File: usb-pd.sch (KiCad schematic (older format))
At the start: 39 parts, among them J12 12401598E4_2A, Q7 SQS401EN-T1_BE3, U18 STUSB4500QTR

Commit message: Reorganize schematics, add descriptions in top left corner
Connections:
- wire segments 133 -> 131
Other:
- note added: "USB-C PD controller"
- note removed: "R G B\n50 30 30 [mA]\n2.1 2.9 2.9 [V]"
- moved on the sheet: C127, C128, C136, C137, C138, C139, D1, D23, D24, D27, D31, J12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

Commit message: Increase spacing between D27 and U18, reduce D27 brightness to ~20%
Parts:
- removed R131: R_100R_0402, sa800u-baseboard-hw-footprints:0402-res, symbol sa800u-baseboard-hw:R_100R_0402
- removed R132: R_150R_0402, sa800u-baseboard-hw-footprints:0402-res, symbol sa800u-baseboard-hw:R_150R_0402
- removed R133: R_590R_0402, sa800u-baseboard-hw-footprints:0402-res, symbol sa800u-baseboard-hw:R_590R_0402
- added R131: R_510R_0402, sa800u-baseboard-hw-footprints:0402-res, symbol sa800u-baseboard-hw:R_510R_0402
- added R132: R_750R_0402, sa800u-baseboard-hw-footprints:0402-res, symbol sa800u-baseboard-hw:R_750R_0402
- added R133: R_2k7_0402, sa800u-baseboard-hw-footprints:0402-res, symbol sa800u-baseboard-hw:R_2k7_0402
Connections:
- wire segments 131 -> 132
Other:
- moved on the sheet: D27
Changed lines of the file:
@@
 Wire Wire Line
 	10225 5525 10225 5900
-Wire Wire Line
-	10925 6825 10925 7050
-Wire Wire Line
-	10725 6825 10725 6950
 $Comp
 L sa800u-baseboard-hw:ASMB-TTF0-0A20B D27
 U 1 1 620BAED1
-P 10925 6175
-F 0 "D27" V 10872 6553 60  0000 L CNN
-F 1 "ASMB-TTF0-0A20B" V 10978 6553 60  0000 L CNN
-F 2 "sa800u-baseboard-hw-footprints:PLCC6_3.5x3.7mm" H 10525 5475 60  0001 L CNN
-F 3 "https://docs.broadcom.com/doc/ASMB-TTF0-0A20B-DS101" H 11125 6475 60  0001 L CNN
-F 4 "ASMB-TTF0-0A20B" H 10475 5575 60  0001 L CNN "MPN"
-F 5 "Broadcom" H 10775 5675 60  0001 L CNN "Manufacturer"
-	1    10925 6175
+P 10925 6600
+F 0 "D27" V 10872 6978 60  0000 L CNN
+F 1 "ASMB-TTF0-0A20B" V 10978 6978 60  0000 L CNN
+F 2 "sa800u-baseboard-hw-footprints:PLCC6_3.5x3.7mm" H 10525 5900 60  0001 L CNN
+F 3 "https://docs.broadcom.com/doc/ASMB-TTF0-0A20B-DS101" H 11125 6900 60  0001 L CNN
+F 4 "ASMB-TTF0-0A20B" H 10475 6000 60  0001 L CNN "MPN"
+F 5 "Broadcom" H 10775 6100 60  0001 L CNN "Manufacturer"
+	1    10925 6600
 	0    1    1    0
 $EndComp
-$Comp
-L sa800u-baseboard-hw:R_100R_0402 R131
-U 1 1 6219BF48
-P 10725 6675
-F 0 "R131" V 10680 6606 60  0000 R CNN
-F 1 "R_100R_0402" H 10725 6525 60  0001 C CNN
-F 2 "sa800u-baseboard-hw-footprints:0402-res" H 10925 6875 60  0001 L CNN
-F 3 "" H 10725 6675 50  0001 C CNN
-F 4 "BOURNS" H 10925 7075 60  0001 L CNN "Manufacturer"
-F 5 "CR0402-FX-1000GLF" H 10925 6975 60  0001 L CNN "MPN"
-F 6 "100R" V 10778 6606 50  0000 R CNN "Val"
-	1    10725 6675
-	0    1    1    0
-$EndComp
-$Comp
-L sa800u-baseboard-hw:R_150R_0402 R132
-U 1 1 62198F27
-P 10925 6675
-F 0 "R132" V 10880 6745 60  0000 L CNN
-F 1 "R_150R_0402" H 10925 6525 60  0001 C CNN
-F 2 "sa800u-baseboard-hw-footprints:0402-res" H 11125 6875 60  0001 L CNN
-F 3 "" H 10925 6675 50  0001 C CNN
-F 4 "VISHAY" H 11125 7075 60  0001 L CNN "Manufacturer"
-F 5 "CRCW0402150RFKED" H 11125 6975 60  0001 L CNN "MPN"
-F 6 "150R" V 10978 6745 50  0000 L CNN "Val"
-	1    10925 6675
-	0    1    1    0
-$EndComp
-Wire Wire Line
-	10725 6525 10725 6425
-Wire Wire Line
-	10925 6425 10925 6525
+Wire Wire Line
+	10725 6950 10725 6850
 $Comp
 L sa800u-baseboard-hw:GND #PWR0230
 U 1 1 62113B31
-P 11325 6825
-F 0 "#PWR0230" H 11325 6575 50  0001 C CNN
-F 1 "GND" H 11330 6652 50  0000 C CNN
-F 2 "" H 11325 6825 50  0001 C CNN
-F 3 "" H 11325 6825 50  0001 C CNN
-	1    11325 6825
-	1    0    0    -1
-$EndComp
-$Comp
-L sa800u-baseboard-hw:R_590R_0402 R133
-U 1 1 621057A9
-P 11325 6675
-F 0 "R133" V 11370 6745 60  0000 L CNN
-F 1 "R_590R_0402" H 11325 6525 60  0001 C CNN
-F 2 "sa800u-baseboard-hw-footprints:0402-res" H 11525 6875 60  0001 L CNN
-F 3 "" H 11325 6675 50  0001 C CNN
-F 4 "PANASONIC_ELECTRONIC_COMPONENTS" H 11525 7075 60  0001 L CNN "Manufacturer"
-F 5 "ERJ2RKF5900X" H 11525 6975 60  0001 L CNN "MPN"
-F 6 "590R" V 11272 6745 50  0000 L CNN "Val"
-	1    11325 6675
-	0    1    -1   0
-$EndComp
-Text GLabel 10675 5875 0    50   Input ~ 0
+P 11125 6900
+F 0 "#PWR0230" H 11125 6650 50  0001 C CNN
+F 1 "GND" H 11130 6727 50  0000 C CNN
+F 2 "" H 11125 6900 50  0001 C CNN
+F 3 "" H 11125 6900 50  0001 C CNN
+	1    11125 6900
+	1    0    0    -1
+$EndComp
+Text GLabel 10675 5900 0    50   Input ~ 0
 5V_SYS
 NoConn ~ 2300 5300
@@
 USB-C PD controller
 Wire Wire Line
-	11325 6475 11325 6525
-Wire Wire Line
-	11125 6425 11125 6475
-Wire Wire Line
-	11125 6475 11325 6475
-Wire Wire Line
-	10675 5875 10725 5875
-Connection ~ 10725 5875
-Wire Wire Line
-	10725 5875 10725 5925
-Wire Wire Line
-	10725 5875 10925 5875
-Wire Wire Line
-	10925 5875 10925 5925
+	11125 6850 11125 6900
 Wire Wire Line
 	9050 5900 10225 5900
 Wire Wire Line
-	10225 5050 11125 5050
-Wire Wire Line
-	11125 5925 11125 5050
+	11125 6350 11125 6300
 Wire Wire Line
 	9050 5900 9050 6200
@@
 	8650 5900 8650 6200
 Wire Wire Line
-	11125 5050 12100 5050
-Connection ~ 11125 5050
+	11300 5950 11300 5050
+Wire Wire Line
+	10725 5950 10725 5900
+Wire Wire Line
+	10725 5900 10675 5900
+Wire Wire Line
+	10725 6250 10725 6350
+Wire Wire Line
+	10925 6250 10925 6350
+Wire Wire Line
+	10725 5900 10925 5900
+Wire Wire Line
+	10925 5900 10925 5950
+Connection ~ 10725 5900
+Wire Wire Line
+	10925 6850 10925 7050
+Wire Wire Line
+	11125 6300 11300 6300
+Wire Wire Line
+	11300 6300 11300 6250
+Connection ~ 11300 5050
+Wire Wire Line
+	11300 5050 12100 5050
+Wire Wire Line
+	10225 5050 11300 5050
+$Comp
+L sa800u-baseboard-hw:R_510R_0402 R131
+U 1 1 66EE9C53
+P 10725 6100
+F 0 "R131" V 10680 6170 60  0000 L CNN
+F 1 "R_510R_0402" H 10725 5950 60  0001 C CNN
+F 2 "sa800u-baseboard-hw-footprints:0402-res" H 10925 6300 60  0001 L CNN
+F 3 "" H 10725 6100 50  0001 C CNN
+F 4 "Yageo" H 10925 6500 60  0001 L CNN "Manufacturer"
+F 5 "RC0402JR-07510RL" H 10925 6400 60  0001 L CNN "MPN"
+F 6 "510R" V 10778 6170 50  0000 L CNN "Val"
+	1    10725 6100
+	0    -1   -1   0
+$EndComp
+$Comp
+L sa800u-baseboard-hw:R_750R_0402 R132
+U 1 1 66EF20C4
+P 10925 6100
+F 0 "R132" V 10880 6170 60  0000 L CNN
+F 1 "R_750R_0402" H 10925 5950 60  0001 C CNN
+F 2 "sa800u-baseboard-hw-footprints:0402-res" H 11125 6300 60  0001 L CNN
+F 3 "" H 10925 6100 50  0001 C CNN
+F 4 "Yageo" H 11125 6500 60  0001 L CNN "Manufacturer"
+F 5 "RC0402FR-07750RL" H 11125 6400 60  0001 L CNN "MPN"
+F 6 "750R" V 10978 6170 50  0000 L CNN "Val"
+	1    10925 6100
+	0    1    1    0
+$EndComp
+$Comp
+L sa800u-baseboard-hw:R_2k7_0402 R133
+U 1 1 66EFB72A
+P 11300 6100
+F 0 "R133" V 11255 6170 60  0000 L CNN
+F 1 "R_2k7_0402" H 11300 5950 60  0001 C CNN
+F 2 "sa800u-baseboard-hw-footprints:0402-res" H 11500 6300 60  0001 L CNN
+F 3 "" H 11300 6100 50  0001 C CNN
+F 4 "KOA" H 11500 6500 60  0001 L CNN "Manufacturer"
+F 5 "RK73H1ETTP2701F" H 11500 6400 60  0001 L CNN "MPN"
+F 6 "2k7" V 11353 6170 50  0000 L CNN "Val"
+	1    11300 6100
+	0    1    1    0
+$EndComp
 $EndSCHEMATC

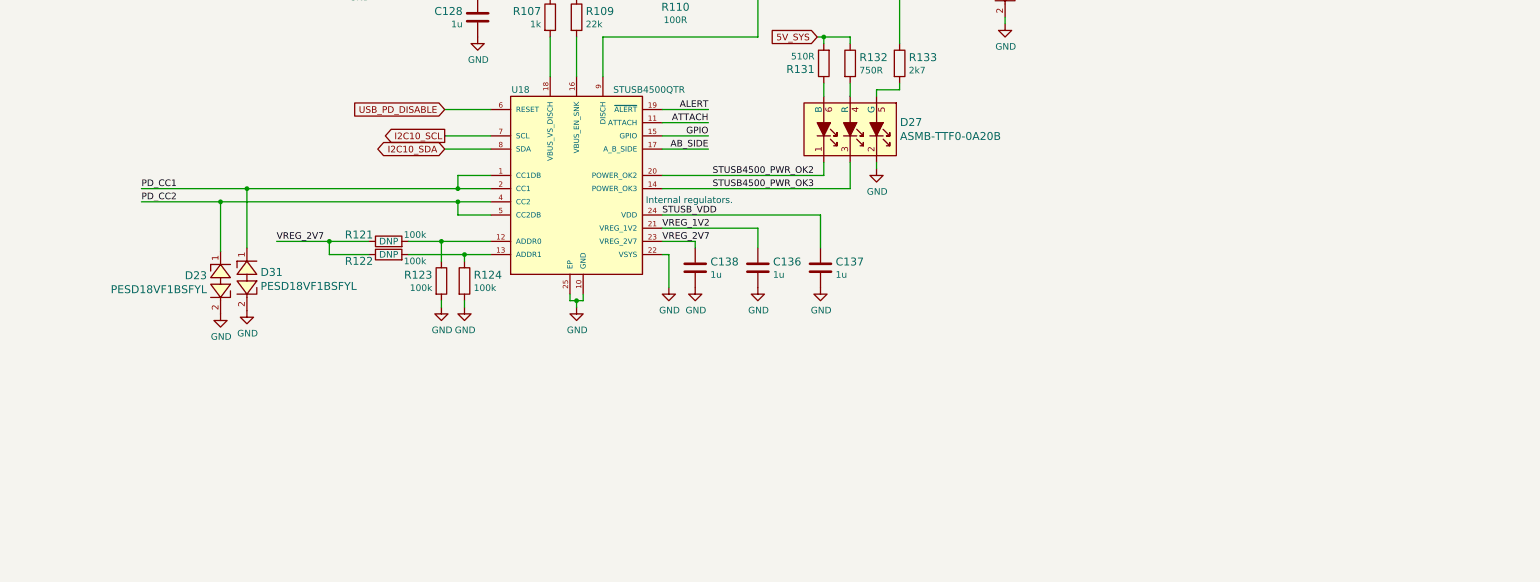
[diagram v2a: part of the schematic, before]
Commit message: Add testpoints to PCB, udpate cache, connect STUSB4500 reset to SoM and pulldown with 10k
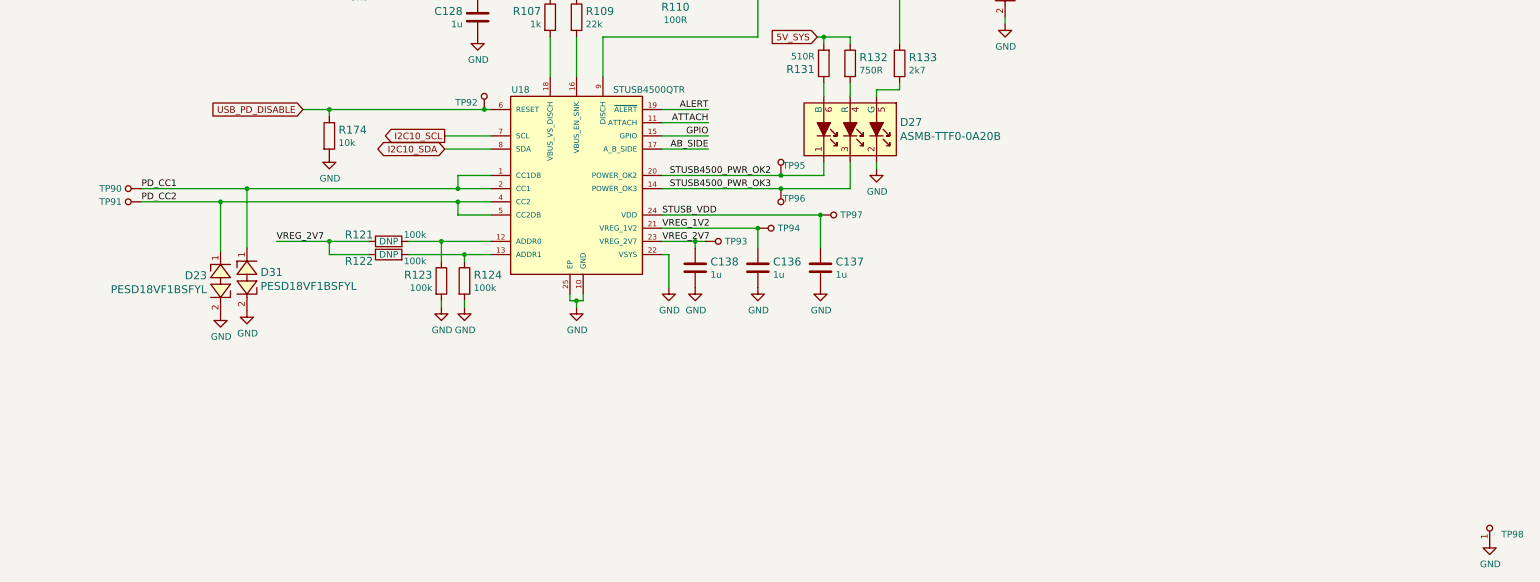
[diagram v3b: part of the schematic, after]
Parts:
- added R174: R_10k_0402, sa800u-baseboard-hw-footprints:0402-res, symbol sa800u-baseboard-hw:R_10k_0402
- added TP90, TP91, TP92, TP93, TP94, TP95, TP96, TP97: TP_SMD_0_75MM, sa800u-baseboard-hw-footprints:Testpoint_smd_0_75mm, symbol sa800u-baseboard-hw:TP_SMD_0_75MM
- added TP98: TP, antmicro-footprints:TP-R-1.5, symbol antmicroTestPoints:TP
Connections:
- net GND: now also R174.2, TP98.1
- net PD_CC1: now also TP90.1
- net PD_CC2: now also TP91.1
- net STUSB4500_PWR_OK2: now also TP95.1
- net STUSB4500_PWR_OK3: now also TP96.1
- net STUSB_VDD: now also TP97.1
- net USB_PD_DISABLE: now also R174.1, TP92.1
- net VREG_1V2: now also TP94.1
- net VREG_2V7: now also TP93.1
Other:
- note removed: "Internal regulators."
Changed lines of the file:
@@
 	8650 5050 8650 5100
 Wire Wire Line
-	8200 6450 7850 6450
-Text GLabel 7850 6450 0    50   Input ~ 0
+	8200 6450 8150 6450
+Text GLabel 6775 6450 0    50   Input ~ 0
 USB_PD_DISABLE
 Wire Wire Line
 	8100 5050 8100 5100
 Connection ~ 8100 5550
-Text Notes 9375 7175 0    50   ~ 0
-Internal regulators.
 $Comp
 L sa800u-baseboard-hw:PMEG6002EJ,115 D24
@@
 Wire Wire Line
 	9850 6750 9500 6750
-Text Label 10650 6950 2    50   ~ 0
+Text Label 10325 6950 2    50   ~ 0
 STUSB4500_PWR_OK2
-Text Label 10650 7050 2    50   ~ 0
+Text Label 10325 7050 2    50   ~ 0
 STUSB4500_PWR_OK3
 Wire Wire Line
@@
 Wire Wire Line
 	9750 7450 9750 7500
-Wire Wire Line
-	9500 7350 10225 7350
-Wire Wire Line
-	10225 7350 10225 7500
 Wire Wire Line
 	9500 7250 10700 7250
@@
 STUSB4500_ALERT
 Wire Wire Line
-	9500 6950 10725 6950
-Wire Wire Line
-	9500 7050 10925 7050
+	9500 6950 10400 6950
 Connection ~ 12100 5050
 Wire Wire Line
@@
 	0    1    1    0
 $EndComp
+$Comp
+L antmicroTestPoints:TP TP?
+U 1 1 69346ED5
+P 15775 9625
+AR Path="/61A19323/69346ED5" Ref="TP?"  Part="1"
+AR Path="/6197686D/69346ED5" Ref="TP?"  Part="1"
+AR Path="/61B0DC30/69346ED5" Ref="TP?"  Part="1"
+AR Path="/61DF77CE/69346ED5" Ref="TP98"  Part="1"
+F 0 "TP98" H 15687 9672 50  0000 R CNN
+F 1 "TP" H 15775 9625 50  0001 C CNN
+F 2 "antmicro-footprints:TP-R-1.5" H 15775 9625 50  0001 C CNN
+F 3 "" H 15775 9625 50  0001 C CNN
+	1    15775 9625
+	-1   0    0    1
+$EndComp
+$Comp
+L sa800u-baseboard-hw:GND #PWR?
+U 1 1 69346EDB
+P 15775 9725
+AR Path="/61BD2CC1/69346EDB" Ref="#PWR?"  Part="1"
+AR Path="/6197686D/69346EDB" Ref="#PWR?"  Part="1"
+AR Path="/61B0DC30/69346EDB" Ref="#PWR?"  Part="1"
+AR Path="/61DF77CE/69346EDB" Ref="#PWR0286"  Part="1"
+F 0 "#PWR0286" H 15775 9475 50  0001 C CNN
+F 1 "GND" H 15780 9552 50  0000 C CNN
+F 2 "" H 15775 9725 50  0001 C CNN
+F 3 "" H 15775 9725 50  0001 C CNN
+	1    15775 9725
+	1    0    0    -1
+$EndComp
+$Comp
+L sa800u-baseboard-hw:TP_SMD_0_75MM TP?
+U 1 1 6935705A
+P 8150 6350
+AR Path="/61B0DC30/6935705A" Ref="TP?"  Part="1"
+AR Path="/61DF77CE/6935705A" Ref="TP92"  Part="1"
+F 0 "TP92" H 8200 6397 50  0000 L CNN
+F 1 "TP_SMD_0_75MM" H 8150 6250 50  0001 C CNN
+F 2 "sa800u-baseboard-hw-footprints:Testpoint_smd_0_75mm" H 8350 6550 60  0001 L CNN
+F 3 "" H 8350 6650 60  0001 L CNN
+	1    8150 6350
+	-1   0    0    1
+$EndComp
+$Comp
+L sa800u-baseboard-hw:TP_SMD_0_75MM TP?
+U 1 1 6936F5F9
+P 10800 7250
+AR Path="/61B0DC30/6936F5F9" Ref="TP?"  Part="1"
+AR Path="/61DF77CE/6936F5F9" Ref="TP97"  Part="1"
+F 0 "TP97" V 10800 7200 50  0000 R CNN
+F 1 "TP_SMD_0_75MM" H 10800 7150 50  0001 C CNN
+F 2 "sa800u-baseboard-hw-footprints:Testpoint_smd_0_75mm" H 11000 7450 60  0001 L CNN
+F 3 "" H 11000 7550 60  0001 L CNN
+	1    10800 7250
+	0    -1   -1   0
+$EndComp
+$Comp
+L sa800u-baseboard-hw:TP_SMD_0_75MM TP?
+U 1 1 69376354
+P 10325 7350
+AR Path="/61B0DC30/69376354" Ref="TP?"  Part="1"
+AR Path="/61DF77CE/69376354" Ref="TP94"  Part="1"
+F 0 "TP94" V 10325 7300 50  0000 R CNN
+F 1 "TP_SMD_0_75MM" H 10325 7250 50  0001 C CNN
+F 2 "sa800u-baseboard-hw-footprints:Testpoint_smd_0_75mm" H 10525 7550 60  0001 L CNN
+F 3 "" H 10525 7650 60  0001 L CNN
+	1    10325 7350
+	0    -1   -1   0
+$EndComp
+$Comp
+L sa800u-baseboard-hw:TP_SMD_0_75MM TP?
+U 1 1 6937AABD
+P 9925 7450
+AR Path="/61B0DC30/6937AABD" Ref="TP?"  Part="1"
+AR Path="/61DF77CE/6937AABD" Ref="TP93"  Part="1"
+F 0 "TP93" V 9925 7400 50  0000 R CNN
+F 1 "TP_SMD_0_75MM" H 9925 7350 50  0001 C CNN
+F 2 "sa800u-baseboard-hw-footprints:Testpoint_smd_0_75mm" H 10125 7650 60  0001 L CNN
+F 3 "" H 10125 7750 60  0001 L CNN
+	1    9925 7450
+	0    -1   -1   0
+$EndComp
+Wire Wire Line
+	9825 7450 9750 7450
+Connection ~ 9750 7450
+Wire Wire Line
+	10225 7350 10225 7500
+Wire Wire Line
+	9500 7350 10225 7350
+Connection ~ 10225 7350
+Connection ~ 10700 7250
+$Comp
+L sa800u-baseboard-hw:TP_SMD_0_75MM TP?
+U 1 1 693AAD1A
+P 10400 7150
+AR Path="/61B0DC30/693AAD1A" Ref="TP?"  Part="1"
+AR Path="/61DF77CE/693AAD1A" Ref="TP96"  Part="1"
+F 0 "TP96" H 10500 7175 50  0000 C CNN
+F 1 "TP_SMD_0_75MM" H 10400 7050 50  0001 C CNN
+F 2 "sa800u-baseboard-hw-footprints:Testpoint_smd_0_75mm" H 10600 7350 60  0001 L CNN
+F 3 "" H 10600 7450 60  0001 L CNN
+	1    10400 7150
+	1    0    0    -1
+$EndComp
+Wire Wire Line
+	9500 7050 10400 7050
+$Comp
+L sa800u-baseboard-hw:TP_SMD_0_75MM TP?
+U 1 1 693DC12F
+P 10400 6850
+AR Path="/61B0DC30/693DC12F" Ref="TP?"  Part="1"
+AR Path="/61DF77CE/693DC12F" Ref="TP95"  Part="1"
+F 0 "TP95" H 10300 6875 50  0000 C CNN
+F 1 "TP_SMD_0_75MM" H 10400 6750 50  0001 C CNN
+F 2 "sa800u-baseboard-hw-footprints:Testpoint_smd_0_75mm" H 10600 7050 60  0001 L CNN
+F 3 "" H 10600 7150 60  0001 L CNN
+	1    10400 6850
+	-1   0    0    1
+$EndComp
+Connection ~ 10400 6950
+Wire Wire Line
+	10400 6950 10725 6950
+Connection ~ 10400 7050
+Wire Wire Line
+	10400 7050 10925 7050
+$Comp
+L sa800u-baseboard-hw:TP_SMD_0_75MM TP?
+U 1 1 6940FE62
+P 5450 7050
+AR Path="/61B0DC30/6940FE62" Ref="TP?"  Part="1"
+AR Path="/61DF77CE/6940FE62" Ref="TP90"  Part="1"
+F 0 "TP90" V 5450 7001 50  0000 R CNN
+F 1 "TP_SMD_0_75MM" H 5450 6950 50  0001 C CNN
+F 2 "sa800u-baseboard-hw-footprints:Testpoint_smd_0_75mm" H 5650 7250 60  0001 L CNN
+F 3 "" H 5650 7350 60  0001 L CNN
+	1    5450 7050
+	0    1    1    0
+$EndComp
+$Comp
+L sa800u-baseboard-hw:TP_SMD_0_75MM TP?
+U 1 1 69414C31
+P 5450 7150
+AR Path="/61B0DC30/69414C31" Ref="TP?"  Part="1"
+AR Path="/61DF77CE/69414C31" Ref="TP91"  Part="1"
+F 0 "TP91" V 5450 7101 50  0000 R CNN
+F 1 "TP_SMD_0_75MM" H 5450 7050 50  0001 C CNN
+F 2 "sa800u-baseboard-hw-footprints:Testpoint_smd_0_75mm" H 5650 7350 60  0001 L CNN
+F 3 "" H 5650 7450 60  0001 L CNN
+	1    5450 7150
+	0    1    1    0
+$EndComp
+Connection ~ 8150 6450
+Wire Wire Line
+	8150 6450 6975 6450
+$Comp
+L sa800u-baseboard-hw:R_10k_0402 R?
+U 1 1 695F4A37
+P 6975 6650
+AR Path="/6197686D/695F4A37" Ref="R?"  Part="1"
+AR Path="/61DF77CE/695F4A37" Ref="R174"  Part="1"
+F 0 "R174" V 6930 6720 60  0000 L CNN
+F 1 "R_10k_0402" H 6975 6500 60  0001 C CNN
+F 2 "sa800u-baseboard-hw-footprints:0402-res" H 7175 6850 60  0001 L CNN
+F 3 "" H 6975 6650 50  0001 C CNN
+F 4 "VISHAY" H 7175 7050 60  0001 L CNN "Manufacturer"
+F 5 "CRCW040210K0FKEDHP" H 7175 6950 60  0001 L CNN "MPN"
+F 6 "10k" V 7028 6720 50  0000 L CNN "Val"
+	1    6975 6650
+	0    1    1    0
+$EndComp
+Wire Wire Line
+	6975 6500 6975 6450
+Connection ~ 6975 6450
+Wire Wire Line
+	6975 6450 6775 6450
+$Comp
+L sa800u-baseboard-hw:GND #PWR0280
+U 1 1 695FF2BD
+P 6975 6800
+F 0 "#PWR0280" H 6975 6550 50  0001 C CNN
+F 1 "GND" H 6980 6627 50  0000 C CNN
+F 2 "" H 6975 6800 50  0001 C CNN
+F 3 "" H 6975 6800 50  0001 C CNN
+	1    6975 6800
+	1    0    0    -1
+$EndComp
 $EndSCHEMATC

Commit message: Clear annotation and annotate
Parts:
- renumbered C127 to C152, C128 to C153, C138 to C154, C139 to C155, C136 to C156, C137 to C157, D23 to D33, D31 to D34, D24 to D35, D27 to D36, D1 to D37, J12 to J11, Q7 to Q17, R174 to R153, R121 to R154, R122 to R155, R123 to R156, R124 to R157, R106 to R158, R107 to R159, R108 to R160, R109 to R161, R161 to R162, R162 to R163, R163 to R164, R164 to R165, R110 to R166, R125 to R167, R126 to R168, R111 to R169, R127 to R170, R131 to R171, R128 to R172, R132 to R173, R133 to R174, TP90 to TP86, TP91 to TP87, TP92 to TP88, TP75 to TP89, TP93 to TP90, TP76 to TP91, TP94 to TP92, TP95 to TP93, TP96 to TP94, TP77 to TP95, TP78 to TP96, U18 to U23

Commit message: Loclib after anotation
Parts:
- TP98: footprint antmicro-footprints:TP-R-1.5 -> sa800u-baseboard-hw-footprints:TP-R-1.5; symbol antmicroTestPoints:TP -> sa800u-baseboard-hw:TP
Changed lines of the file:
@@
 $EndComp
 $Comp
-L antmicroTestPoints:TP TP?
+L sa800u-baseboard-hw:TP TP?
 U 1 1 69346ED5
 P 15775 9625
@@
 F 0 "TP98" H 15687 9672 50  0000 R CNN
 F 1 "TP" H 15775 9625 50  0001 C CNN
-F 2 "antmicro-footprints:TP-R-1.5" H 15775 9625 50  0001 C CNN
+F 2 "sa800u-baseboard-hw-footprints:TP-R-1.5" H 15775 9625 50  0001 C CNN
 F 3 "" H 15775 9625 50  0001 C CNN
 	1    15775 9625

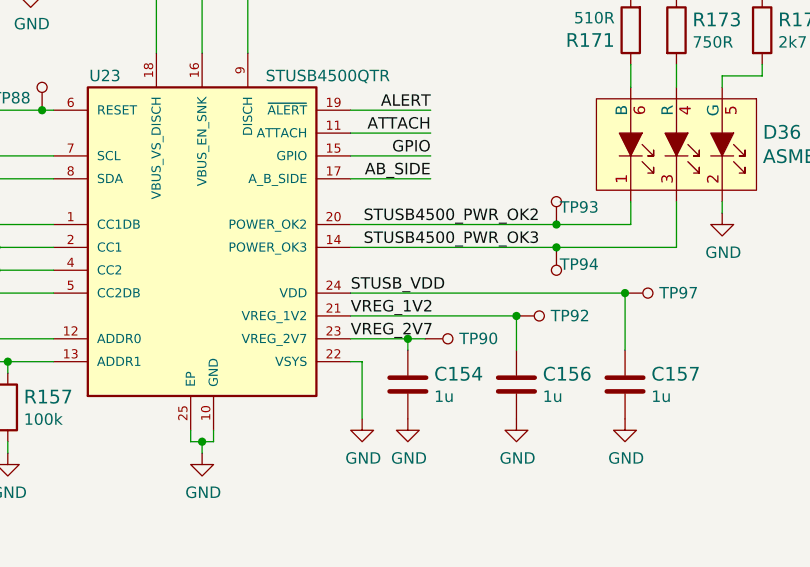
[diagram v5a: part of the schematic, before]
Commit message: Add missing connection to Vbus on STUSB4500
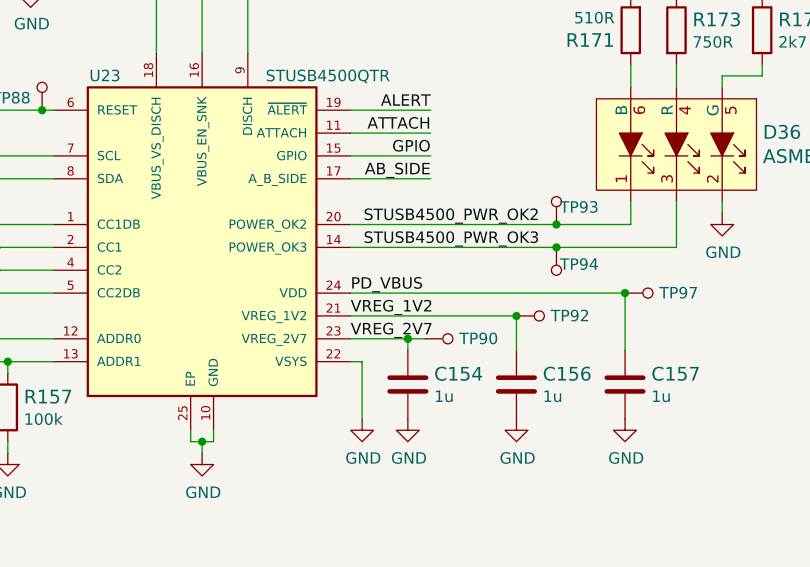
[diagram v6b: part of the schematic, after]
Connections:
- net STUSB_VDD is gone; now on net PD_VBUS: C157.1, TP97.1, U23.24 (VDD)
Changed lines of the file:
@@
 Text Label 9500 7350 0    50   ~ 0
 VREG_1V2
-Text Label 9500 7250 0    50   ~ 0
-STUSB_VDD
 Connection ~ 8100 5050
 Wire Wire Line
@@
 	1    0    0    -1
 $EndComp
+Text Label 9500 7250 0    50   ~ 0
+PD_VBUS
 $EndSCHEMATC
